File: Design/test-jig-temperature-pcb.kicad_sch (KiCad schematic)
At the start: 44 parts, among them J1 Jack-DC, J10 Thermistor, J2 SWD, J3 Thermistor, J4 Thermistor, J5 Thermistor, J6 Thermistor, J7 Thermistor, J8 Thermistor, J9 Thermistor, Q1 BC547, U1 STM32G030C6Tx, U2 TL1117B-3.3

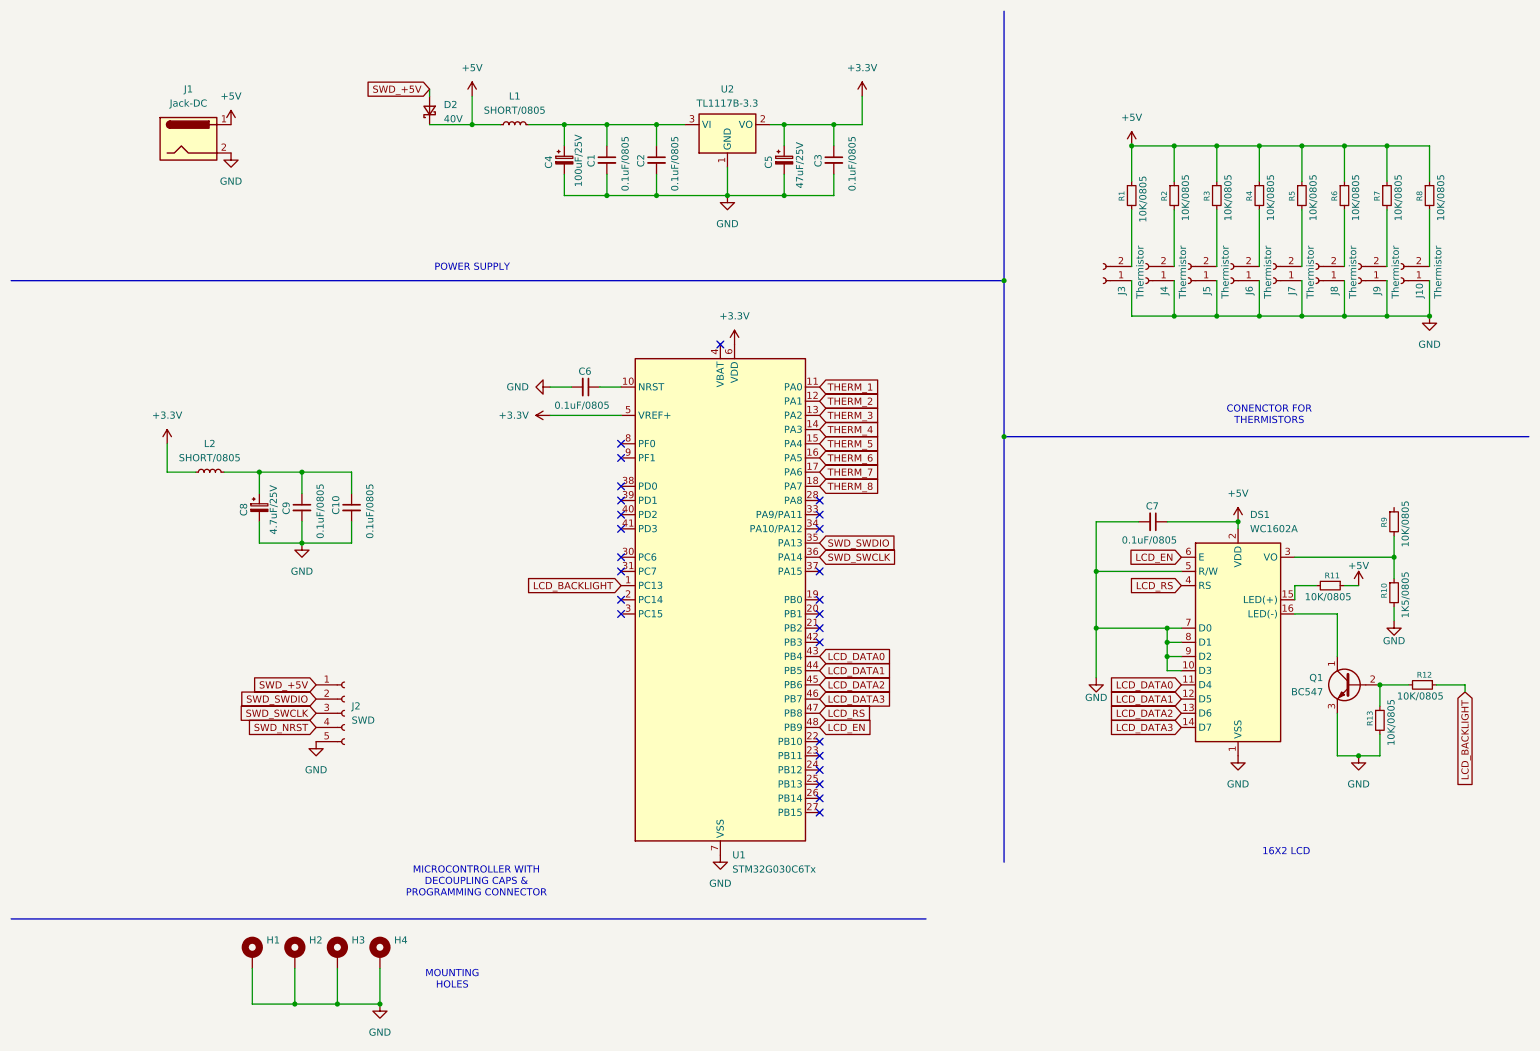
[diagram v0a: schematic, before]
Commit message: Fix ERC issues and re-annotate schematic
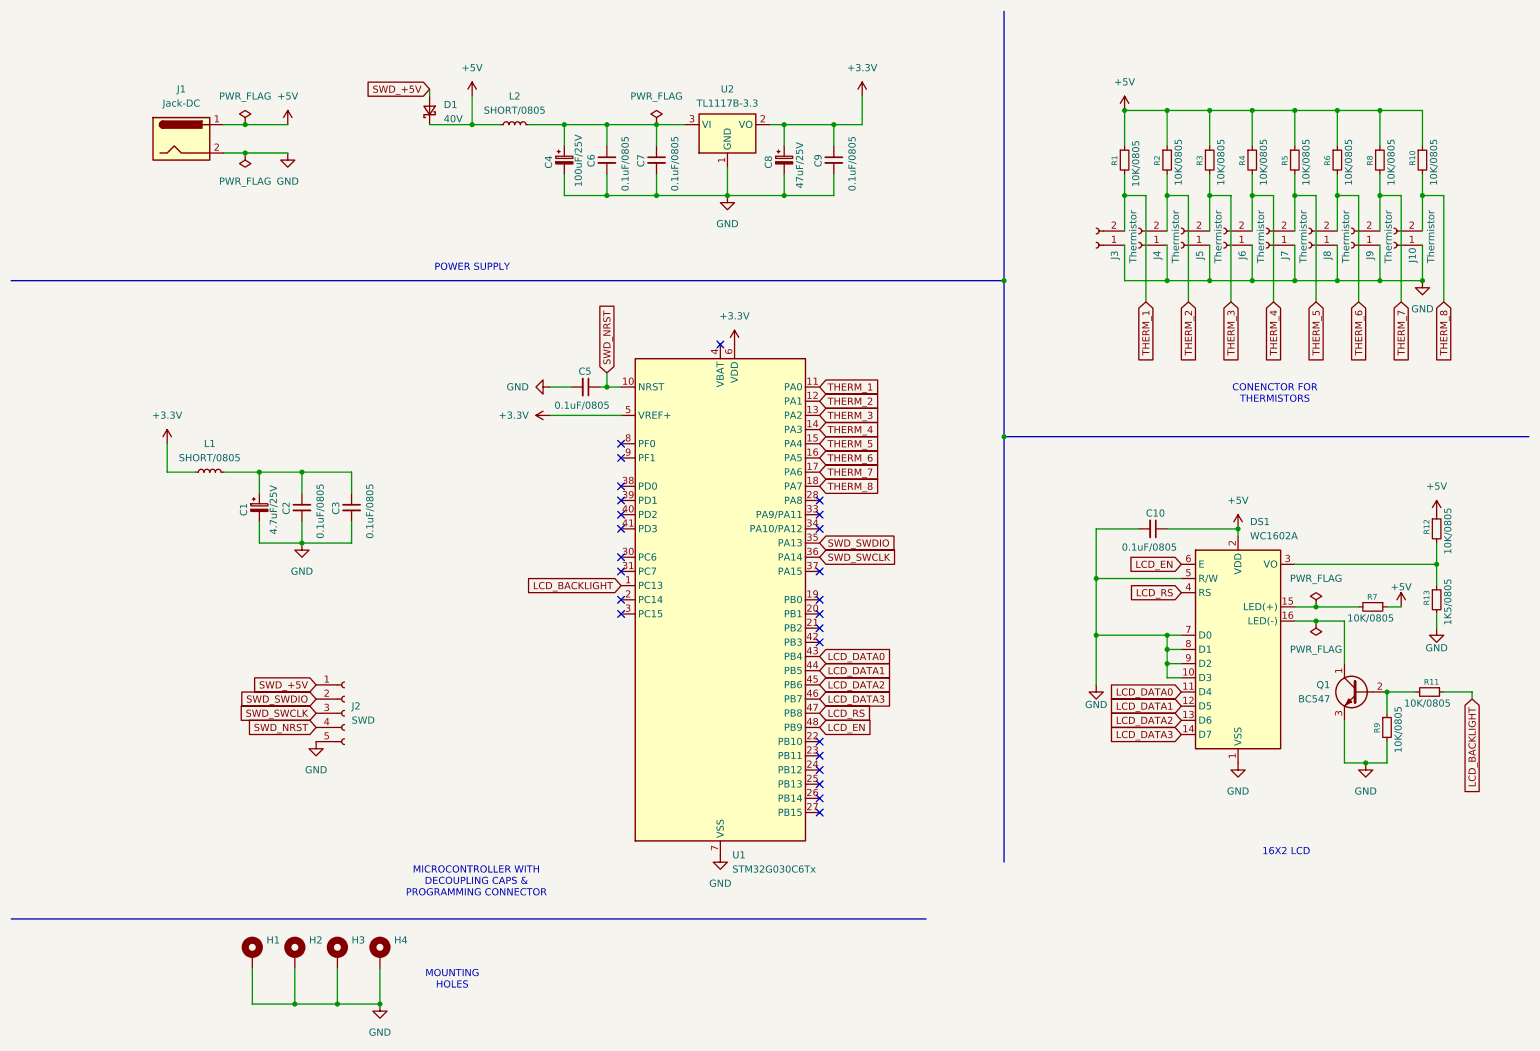
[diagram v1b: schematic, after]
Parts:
- renumbered C8 to C1, C7 to C10, C9 to C2, C10 to C3, C6 to C5, C1 to C6, C2 to C7, C5 to C8, C3 to C9, D2 to D1, L2 to L1, L1 to L2, R8 to R10, R12 to R11, R9 to R12, R10 to R13, R11 to R7, R7 to R8, R13 to R9
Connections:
- net +5V: now also R12.1
- net SWD_NRST: now also C5.1, U1.10 (NRST)
- net THERM_1: now also J3.2 (Pin_2), R1.2
- net THERM_2: now also J4.2 (Pin_2), R2.2
- net THERM_3: now also J5.2 (Pin_2), R3.2
- net THERM_4: now also J6.2 (Pin_2), R4.2
- net THERM_5: now also J7.2 (Pin_2), R5.2
- net THERM_6: now also J8.2 (Pin_2), R6.2
- net THERM_7: now also J9.2 (Pin_2), R8.2
- net THERM_8: now also J10.2 (Pin_2), R10.2
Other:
- moved on the sheet: C10, DS1, J1, J10, J3, J4, J5, J6, J7, J8, J9, Q1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

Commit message: Assign footprints to symbols
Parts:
- C1, C4, C8: footprint (none) -> Capacitor_THT:CP_Radial_D5.0mm_P2.00mm
- C10, C2, C3, C5, C6, C7, C9: footprint (none) -> Capacitor_SMD:C_0805_2012Metric_Pad1.18x1.45mm_HandSolder
- D1: footprint (none) -> Diode_SMD:D_SMA_Handsoldering
- H1, H2, H3, H4: footprint (none) -> MountingHole:MountingHole_2.5mm_Pad
- J1: footprint (none) -> Connector_BarrelJack:BarrelJack_Horizontal
- J10, J3, J4, J5, J6, J7, J8, J9: footprint (none) -> Connector_JST:JST_XH_B2B-XH-A_1x02_P2.50mm_Vertical
- J2: footprint (none) -> Connector_JST:JST_XH_B5B-XH-A_1x05_P2.50mm_Vertical
- L1, L2, R1, R10, R11, R12, R13, R2, R3, R4, R5, R6, R7, R8, R9: footprint (none) -> Resistor_SMD:R_0805_2012Metric_Pad1.20x1.40mm_HandSolder
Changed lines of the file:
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@@
 			)
 		)
-		(property "Footprint" ""
+		(property "Footprint" "Capacitor_SMD:C_0805_2012Metric_Pad1.18x1.45mm_HandSolder"
 			(at 73.66 101.6 0)
 			(effects
@@
 			)
 		)
-		(property "Footprint" ""
+		(property "Footprint" "Capacitor_THT:CP_Radial_D5.0mm_P2.00mm"
 			(at 111.76 39.37 0)
 			(effects
@@
 			)
 		)
-		(property "Footprint" ""
+		(property "Footprint" "Resistor_SMD:R_0805_2012Metric_Pad1.20x1.40mm_HandSolder"
 			(at 257.81 39.37 0)
 			(effects
@@
 			)
 		)
-		(property "Footprint" ""
+		(property "Footprint" "Connector_BarrelJack:BarrelJack_Horizontal"
 			(at 44.45 36.576 0)
 			(effects
@@
 			)
 		)
-		(property "Footprint" ""
+		(property "Footprint" "Resistor_SMD:R_0805_2012Metric_Pad1.20x1.40mm_HandSolder"
 			(at 267.97 118.11 0)
 			(effects
@@
 			)
 		)
-		(property "Footprint" ""
+		(property "Footprint" "Resistor_SMD:R_0805_2012Metric_Pad1.20x1.40mm_HandSolder"
 			(at 227.33 39.37 0)
 			(effects
@@
 			)
 		)
-		(property "Footprint" ""
+		(property "Footprint" "Connector_JST:JST_XH_B2B-XH-A_1x02_P2.50mm_Vertical"
 			(at 237.49 54.61 0)
 			(effects
@@
 			)
 		)
-		(property "Footprint" ""
+		(property "Footprint" "Connector_JST:JST_XH_B2B-XH-A_1x02_P2.50mm_Vertical"
 			(at 214.63 54.61 0)
 			(effects
@@
 			)
 		)
-		(property "Footprint" ""
+		(property "Footprint" "MountingHole:MountingHole_2.5mm_Pad"
 			(at 78.74 181.61 0)
 			(effects
@@
 			)
 		)
-		(property "Footprint" ""
+		(property "Footprint" "Capacitor_SMD:C_0805_2012Metric_Pad1.18x1.45mm_HandSolder"
 			(at 119.38 39.37 0)
 			(effects
@@
 			)
 		)
-		(property "Footprint" ""
+		(property "Footprint" "Resistor_SMD:R_0805_2012Metric_Pad1.20x1.40mm_HandSolder"
 			(at 212.09 39.37 0)
 			(effects
@@
 			)
 		)
-		(property "Footprint" ""
+		(property "Footprint" "Connector_JST:JST_XH_B2B-XH-A_1x02_P2.50mm_Vertical"
 			(at 245.11 54.61 0)
 			(effects
@@
 			)
 		)
-		(property "Footprint" ""
+		(property "Footprint" "Capacitor_THT:CP_Radial_D5.0mm_P2.00mm"
 			(at 151.13 39.37 0)
 			(effects
@@
 			)
 		)
-		(property "Footprint" ""
+		(property "Footprint" "Capacitor_SMD:C_0805_2012Metric_Pad1.18x1.45mm_HandSolder"
 			(at 115.57 80.01 0)
 			(effects
@@
 			)
 		)
-		(property "Footprint" ""
+		(property "Footprint" "Resistor_SMD:R_0805_2012Metric_Pad1.20x1.40mm_HandSolder"
 			(at 266.7 134.62 0)
 			(effects
@@
 			)
 		)
-		(property "Footprint" ""
+		(property "Footprint" "Capacitor_THT:CP_Radial_D5.0mm_P2.00mm"
 			(at 57.15 101.6 0)
 			(effects
@@
 			)
 		)
-		(property "Footprint" ""
+		(property "Footprint" "Capacitor_SMD:C_0805_2012Metric_Pad1.18x1.45mm_HandSolder"
 			(at 128.27 39.37 0)
 			(effects
@@
 			)
 		)
-		(property "Footprint" ""
+		(property "Footprint" "Resistor_SMD:R_0805_2012Metric_Pad1.20x1.40mm_HandSolder"
 			(at 267.97 105.41 0)
 			(effects
@@
 			)
 		)
-		(property "Footprint" ""
+		(property "Footprint" "Resistor_SMD:R_0805_2012Metric_Pad1.20x1.40mm_HandSolder"
 			(at 219.71 39.37 0)
 			(effects
@@
 			)
 		)
-		(property "Footprint" ""
+		(property "Footprint" "Connector_JST:JST_XH_B2B-XH-A_1x02_P2.50mm_Vertical"
 			(at 222.25 54.61 0)
 			(effects
@@
 			)
 		)
-		(property "Footprint" ""
+		(property "Footprint" "Resistor_SMD:R_0805_2012Metric_Pad1.20x1.40mm_HandSolder"
 			(at 102.87 33.02 0)
 			(effects
@@
 			)
 		)
-		(property "Footprint" ""
+		(property "Footprint" "Connector_JST:JST_XH_B5B-XH-A_1x05_P2.50mm_Vertical"
 			(at 72.39 138.43 0)
 			(effects
@@
 			)
 		)
-		(property "Footprint" ""
+		(property "Footprint" "Resistor_SMD:R_0805_2012Metric_Pad1.20x1.40mm_HandSolder"
 			(at 265.43 39.37 0)
 			(effects
@@
 			)
 		)
-		(property "Footprint" ""
+		(property "Footprint" "Connector_JST:JST_XH_B2B-XH-A_1x02_P2.50mm_Vertical"
 			(at 252.73 54.61 0)
 			(effects
@@
 			)
 		)
-		(property "Footprint" ""
+		(property "Footprint" "Resistor_SMD:R_0805_2012Metric_Pad1.20x1.40mm_HandSolder"
 			(at 242.57 39.37 0)
 			(effects
@@
 			)
 		)
-		(property "Footprint" ""
+		(property "Footprint" "Capacitor_SMD:C_0805_2012Metric_Pad1.18x1.45mm_HandSolder"
 			(at 160.02 39.37 0)
 			(effects
@@
 			)
 		)
-		(property "Footprint" ""
+		(property "Footprint" "Capacitor_SMD:C_0805_2012Metric_Pad1.18x1.45mm_HandSolder"
 			(at 64.77 101.6 0)
 			(effects
@@
 			)
 		)
-		(property "Footprint" ""
+		(property "Footprint" "MountingHole:MountingHole_2.5mm_Pad"
 			(at 63.5 181.61 0)
 			(effects
@@
 			)
 		)
-		(property "Footprint" ""
+		(property "Footprint" "Resistor_SMD:R_0805_2012Metric_Pad1.20x1.40mm_HandSolder"
 			(at 234.95 39.37 0)
 			(effects
@@
 			)
 		)
-		(property "Footprint" ""
+		(property "Footprint" "Connector_JST:JST_XH_B2B-XH-A_1x02_P2.50mm_Vertical"
 			(at 207.01 54.61 0)
 			(effects
@@
 			)
 		)
-		(property "Footprint" ""
+		(property "Footprint" "Resistor_SMD:R_0805_2012Metric_Pad1.20x1.40mm_HandSolder"
 			(at 48.26 95.25 0)
 			(effects
@@
 			)
 		)
-		(property "Footprint" ""
+		(property "Footprint" "MountingHole:MountingHole_2.5mm_Pad"
 			(at 71.12 181.61 0)
 			(effects
@@
 			)
 		)
-		(property "Footprint" ""
+		(property "Footprint" "Resistor_SMD:R_0805_2012Metric_Pad1.20x1.40mm_HandSolder"
 			(at 256.54 119.38 0)
 			(effects
@@
 			)
 		)
-		(property "Footprint" ""
+		(property "Footprint" "Resistor_SMD:R_0805_2012Metric_Pad1.20x1.40mm_HandSolder"
 			(at 259.08 140.97 0)
 			(effects
@@
 			)
 		)
-		(property "Footprint" ""
+		(property "Footprint" "Capacitor_SMD:C_0805_2012Metric_Pad1.18x1.45mm_HandSolder"
 			(at 217.17 105.41 0)
 			(effects
@@
 			)
 		)
-		(property "Footprint" ""
+		(property "Footprint" "Diode_SMD:D_SMA_Handsoldering"
 			(at 87.63 30.48 90)
 			(effects
@@
 			)
 		)
-		(property "Footprint" ""
+		(property "Footprint" "MountingHole:MountingHole_2.5mm_Pad"
 			(at 55.88 181.61 0)
 			(effects
@@
 			)
 		)
-		(property "Footprint" ""
+		(property "Footprint" "Connector_JST:JST_XH_B2B-XH-A_1x02_P2.50mm_Vertical"
 			(at 229.87 54.61 0)
 			(effects
@@
 			)
 		)
-		(property "Footprint" ""
+		(property "Footprint" "Connector_JST:JST_XH_B2B-XH-A_1x02_P2.50mm_Vertical"
 			(at 260.35 54.61 0)
 			(effects
@@
 			)
 		)
-		(property "Footprint" ""
+		(property "Footprint" "Resistor_SMD:R_0805_2012Metric_Pad1.20x1.40mm_HandSolder"
 			(at 250.19 39.37 0)
 			(effects

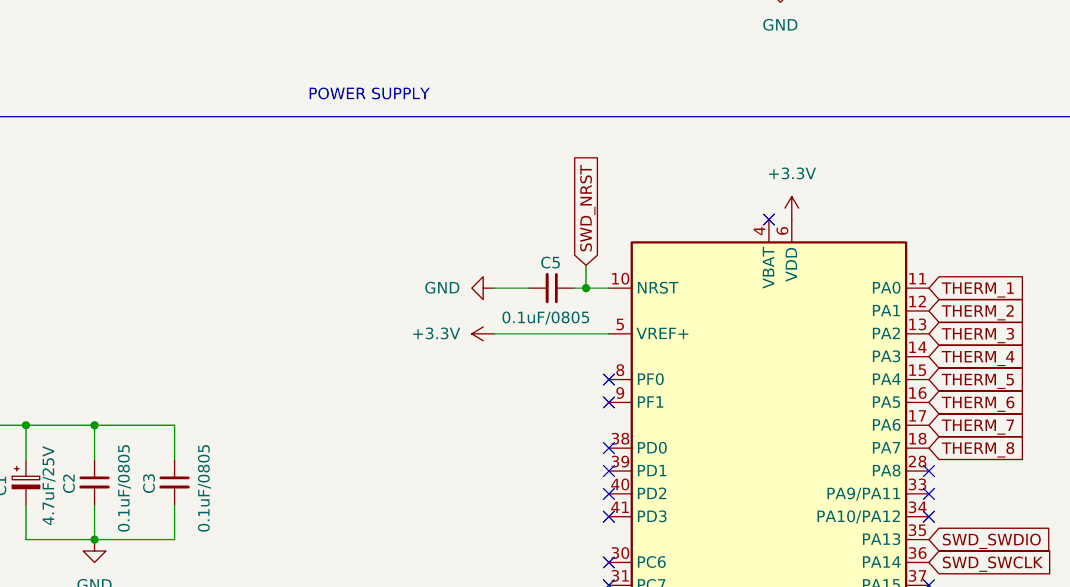
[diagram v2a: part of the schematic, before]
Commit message: Group components and route thermistor connector to MCU
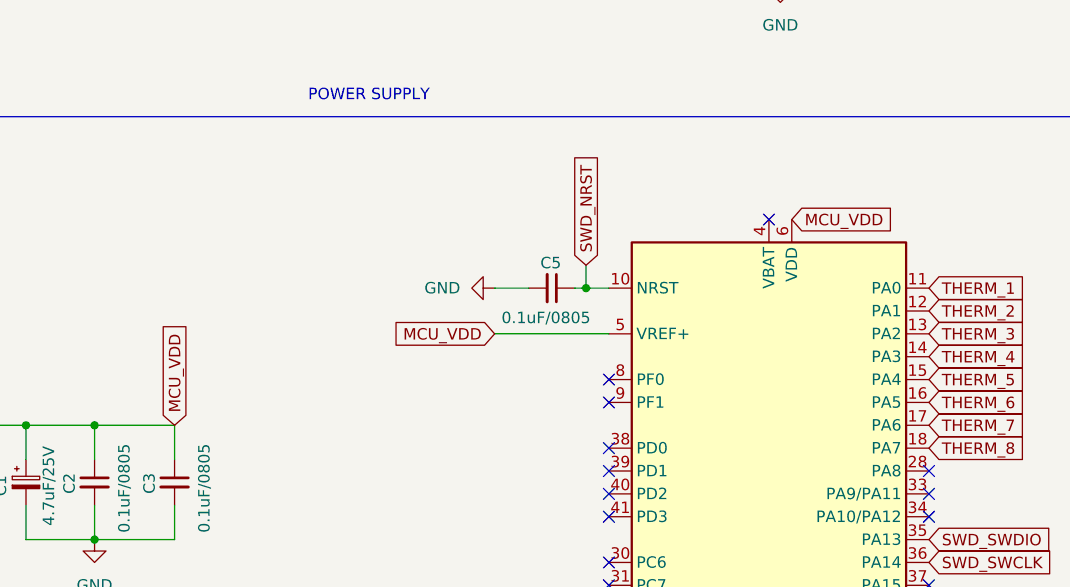
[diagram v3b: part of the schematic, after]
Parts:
- Q1: footprint Package_TO_SOT_THT:TO-92_Inline -> Package_TO_SOT_SMD:SOT-23
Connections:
- net +3.3V: no longer U1.5 (VREF+), U1.6 (VDD)
- net MCU_VDD: now reaches C1.1, C2.1, C3.1, L1.2
- net MCU_VDD: now also U1.5 (VREF+), U1.6 (VDD)
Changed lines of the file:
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@@
 		)
 	)
+	(global_label "MCU_VDD"
+		(shape input)
+		(at 109.22 85.09 180)
+		(fields_autoplaced yes)
+		(effects
+			(font
+				(size 1.27 1.27)
+			)
+			(justify right)
+		)
+		(property "Intersheetrefs" "${INTERSHEET_REFS}"
+			(at 97.5867 85.09 0)
+			(effects
+				(font
+					(size 1.27 1.27)
+				)
+				(justify right)
+				(hide yes)
+			)
+		)
+	)
 	(global_label "THERM_1"
 		(shape input)
@@
 		)
 	)
+	(global_label "MCU_VDD"
+		(shape input)
+		(at 142.24 72.39 0)
+		(fields_autoplaced yes)
+		(effects
+			(font
+				(size 1.27 1.27)
+			)
+			(justify left)
+		)
+		(property "Intersheetrefs" "${INTERSHEET_REFS}"
+			(at 153.8733 72.39 0)
+			(effects
+				(font
+					(size 1.27 1.27)
+				)
+				(justify left)
+				(hide yes)
+			)
+		)
+	)
 	(global_label "LCD_DATA0"
 		(shape input)
@@
 		)
 	)
+	(global_label "MCU_VDD"
+		(shape input)
+		(at 73.66 95.25 90)
+		(fields_autoplaced yes)
+		(effects
+			(font
+				(size 1.27 1.27)
+			)
+			(justify left)
+		)
+		(property "Intersheetrefs" "${INTERSHEET_REFS}"
+			(at 73.66 83.6167 90)
+			(effects
+				(font
+					(size 1.27 1.27)
+				)
+				(justify left)
+				(hide yes)
+			)
+		)
+	)
 	(symbol
 		(lib_id "Device:C_Small")
@@
 			)
 		)
-		(property "Footprint" "Package_TO_SOT_THT:TO-92_Inline"
+		(property "Footprint" "Package_TO_SOT_SMD:SOT-23"
 			(at 248.92 136.525 0)
 			(effects
@@
 	)
 	(symbol
-		(lib_id "power:+3.3V")
-		(at 142.24 72.39 0)
-		(unit 1)
-		(exclude_from_sim no)
-		(in_bom yes)
-		(on_board yes)
-		(dnp no)
-		(fields_autoplaced yes)
-		(property "Reference" "#PWR012"
-			(at 142.24 76.2 0)
-			(effects
-				(font
-					(size 1.27 1.27)
-				)
-				(hide yes)
-			)
-		)
-		(property "Value" "+3.3V"
-			(at 142.24 67.31 0)
-			(effects
-				(font
-					(size 1.27 1.27)
-				)
-			)
-		)
-		(property "Footprint" ""
-			(at 142.24 72.39 0)
-			(effects
-				(font
-					(size 1.27 1.27)
-				)
-				(hide yes)
-			)
-		)
-		(property "Datasheet" ""
-			(at 142.24 72.39 0)
-			(effects
-				(font
-					(size 1.27 1.27)
-				)
-				(hide yes)
-			)
-		)
-		(property "Description" "Power symbol creates a global label with name \"+3.3V\""
-			(at 142.24 72.39 0)
-			(effects
-				(font
-					(size 1.27 1.27)
-				)
-				(hide yes)
-			)
-		)
-		(pin "1"
-		)
-		(instances
-			(project ""
-				(path "/ee90df8d-0f55-4797-b97b-555aec38ead9"
-					(reference "#PWR012")
-					(unit 1)
-				)
-			)
-		)
-	)
-	(symbol
 		(lib_id "power:PWR_FLAG")
 		(at 128.27 33.02 0)
@@
 					(unit 1)
 				)
-			)
-		)
-	)
-	(symbol
-		(lib_id "power:+3.3V")
-		(at 109.22 85.09 90)
-		(unit 1)
-		(exclude_from_sim no)
-		(in_bom yes)
-		(on_board yes)
-		(dnp no)
-		(fields_autoplaced yes)
-		(property "Reference" "#PWR09"
-			(at 113.03 85.09 0)
-			(effects
-				(font
-					(size 1.27 1.27)
-				)
-				(hide yes)
-			)
-		)
-		(property "Value" "+3.3V"
-			(at 105.41 85.0899 90)
-			(effects
-				(font
-					(size 1.27 1.27)
-				)
-				(justify left)
-			)
-		)
-		(property "Footprint" ""
-			(at 109.22 85.09 0)
-			(effects
-				(font
-					(size 1.27 1.27)
-				)
-				(hide yes)
-			)
-		)
-		(property "Datasheet" ""
-			(at 109.22 85.09 0)
-			(effects
-				(font
-					(size 1.27 1.27)
-				)
-				(hide yes)
-			)
-		)
-		(property "Description" "Power symbol creates a global label with name \"+3.3V\""
-			(at 109.22 85.09 0)
-			(effects
-				(font
-					(size 1.27 1.27)
-				)
-				(hide yes)
-			)
-		)
-		(pin "1"
-		)
-		(instances
-			(project ""
-				(path "/ee90df8d-0f55-4797-b97b-555aec38ead9"
-					(reference "#PWR09")
-					(unit 1)
-				)
